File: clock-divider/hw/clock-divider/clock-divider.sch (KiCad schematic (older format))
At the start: 48 parts

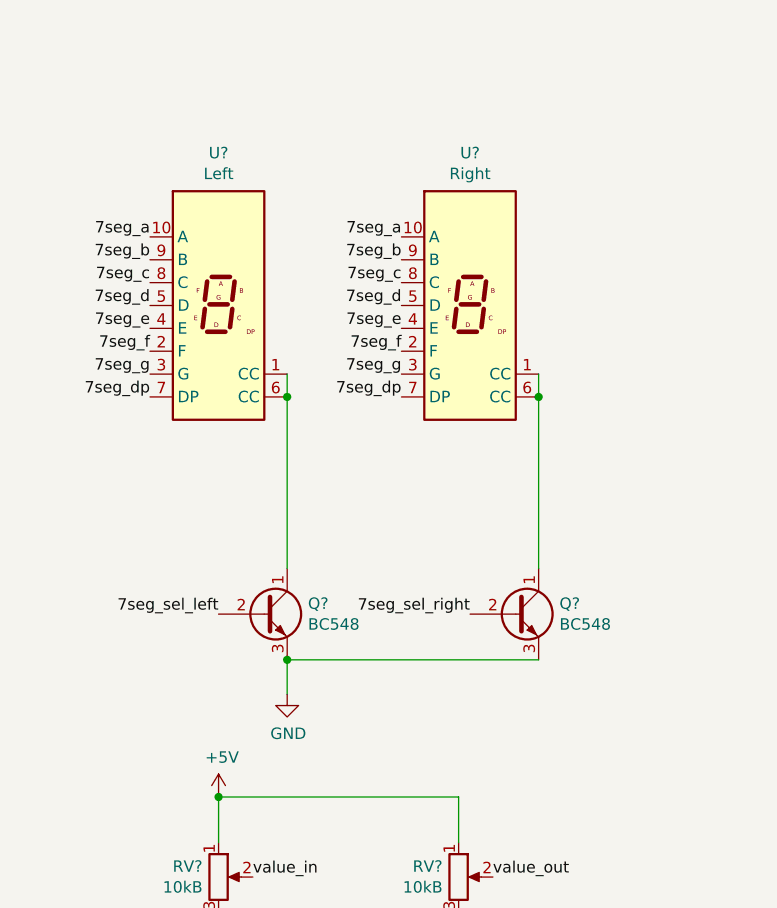
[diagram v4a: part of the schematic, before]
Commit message: clock-divider: change 7 segment display to common anode
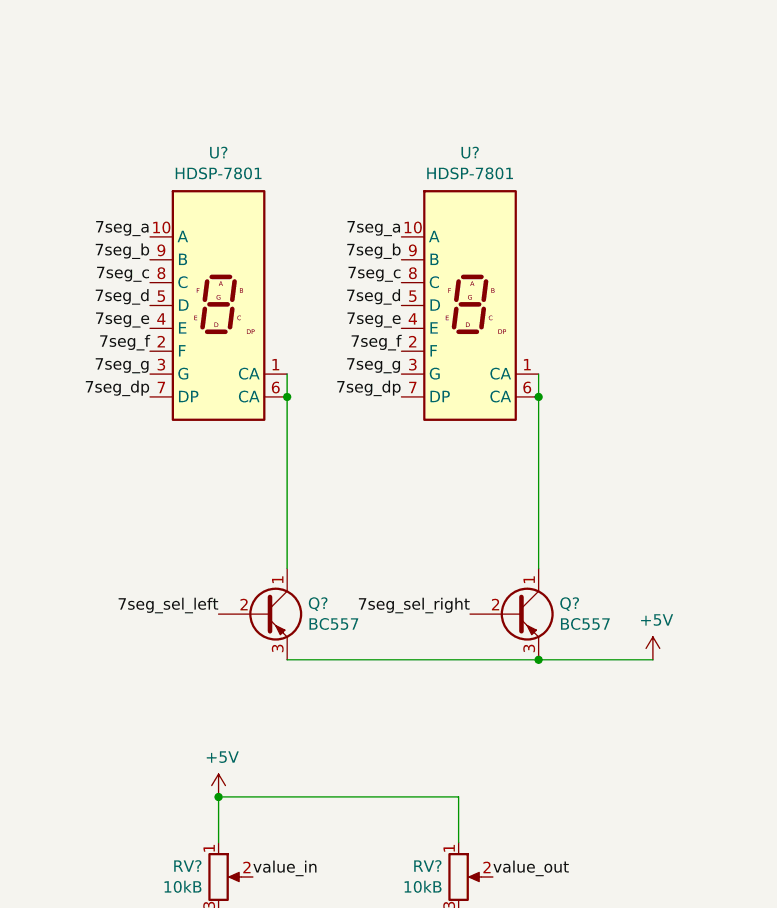
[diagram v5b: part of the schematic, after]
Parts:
- removed Q? (x2): BC548, Package_TO_SOT_THT:TO-92_Inline, symbol Transistor_BJT:BC548
- removed U?: Left, Display_7Segment:HDSP-7801, symbol Display_Character:HDSP-7803
- removed U?: Right, Display_7Segment:HDSP-7801, symbol Display_Character:HDSP-7803
- added Q? (x2): BC557, Package_TO_SOT_THT:TO-92_Inline, symbol Transistor_BJT:BC557
- added U? (x2): HDSP-7801, Display_7Segment:HDSP-7801, symbol Display_Character:HDSP-7801
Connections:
- net +5V: now also Q?.3 (E), Q?.3 (E)
- net 7seg_a: now also U?.10 (A), U?.10 (A)
- net 7seg_b: now also U?.9 (B), U?.9 (B)
- net 7seg_c: now also U?.8 (C), U?.8 (C)
- net 7seg_d: now also U?.5 (D), U?.5 (D)
- net 7seg_dp: now also U?.7 (DP), U?.7 (DP)
- net 7seg_e: now also U?.4 (E), U?.4 (E)
- net 7seg_f: now also U?.2 (F), U?.2 (F)
- net 7seg_g: now also U?.3 (G), U?.3 (G)
- net 7seg_sel_left: now also Q?.2 (B)
- net 7seg_sel_right: now also Q?.2 (B)
- new net: Q?.1 (C), U?.1 (CA), U?.6 (CA) (x2)
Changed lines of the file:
@@
 Connection ~ 4400 1500
-$Comp
-L Display_Character:HDSP-7803 U?
-U 1 1 60601416
-P 8550 2100
-F 0 "U?" H 8550 2767 50  0000 C CNN
-F 1 "Left" H 8550 2676 50  0000 C CNN
-F 2 "Display_7Segment:HDSP-7801" H 8550 1550 50  0001 C CNN
-F 3 "https://docs.broadcom.com/docs/AV02-2553EN" H 8550 2100 50  0001 C CNN
-	1    8550 2100
-	1    0    0    -1
-$EndComp
-$Comp
-L Display_Character:HDSP-7803 U?
-U 1 1 60603731
-P 9650 2100
-F 0 "U?" H 9650 2767 50  0000 C CNN
-F 1 "Right" H 9650 2676 50  0000 C CNN
-F 2 "Display_7Segment:HDSP-7801" H 9650 1550 50  0001 C CNN
-F 3 "https://docs.broadcom.com/docs/AV02-2553EN" H 9650 2100 50  0001 C CNN
-	1    9650 2100
-	1    0    0    -1
-$EndComp
-$Comp
-L Transistor_BJT:BC548 Q?
-U 1 1 60604B60
-P 8750 3450
-F 0 "Q?" H 8941 3496 50  0000 L CNN
-F 1 "BC548" H 8941 3405 50  0000 L CNN
-F 2 "Package_TO_SOT_THT:TO-92_Inline" H 8950 3375 50  0001 L CIN
-F 3 "https://www.onsemi.com/pub/Collateral/BC550-D.pdf" H 8750 3450 50  0001 L CNN
-	1    8750 3450
-	1    0    0    -1
-$EndComp
-$Comp
-L Transistor_BJT:BC548 Q?
-U 1 1 60605442
-P 9850 3450
-F 0 "Q?" H 10041 3496 50  0000 L CNN
-F 1 "BC548" H 10041 3405 50  0000 L CNN
-F 2 "Package_TO_SOT_THT:TO-92_Inline" H 10050 3375 50  0001 L CIN
-F 3 "https://www.onsemi.com/pub/Collateral/BC550-D.pdf" H 9850 3450 50  0001 L CNN
-	1    9850 3450
-	1    0    0    -1
-$EndComp
 $Comp
 L Device:R_POT RV?
@@
 Text Label 9400 5650 2    50   ~ 0
 act_out
-Wire Wire Line
-	8850 2400 8850 2500
-Connection ~ 8850 2500
-Wire Wire Line
-	9950 3250 9950 2500
-Connection ~ 9950 2500
-Wire Wire Line
-	9950 2500 9950 2400
 Text Label 9350 1800 2    50   ~ 0
 7seg_a
@@
 Text Label 10400 5650 2    50   ~ 0
 disp_next_seq
-$Comp
-L power:GND #PWR?
-U 1 1 6078B251
-P 8850 3800
-F 0 "#PWR?" H 8850 3550 50  0001 C CNN
-F 1 "GND" H 8855 3627 50  0000 C CNN
-F 2 "" H 8850 3800 50  0001 C CNN
-F 3 "" H 8850 3800 50  0001 C CNN
-	1    8850 3800
-	1    0    0    -1
-$EndComp
 Wire Wire Line
 	9950 3650 8850 3650
-Wire Wire Line
-	8850 3650 8850 3800
-Connection ~ 8850 3650
 $Comp
 L Device:R R?
@@
 	0    1    1    0
 $EndComp
-Wire Wire Line
-	8850 2500 8850 3250
 Text Label 9650 3450 2    50   ~ 0
 7seg_sel_right
@@
 NoConn ~ 1150 1100
 NoConn ~ 1150 1200
+$Comp
+L Display_Character:HDSP-7801 U?
+U 1 1 60924FDA
+P 9650 2100
+F 0 "U?" H 9650 2767 50  0000 C CNN
+F 1 "HDSP-7801" H 9650 2676 50  0000 C CNN
+F 2 "Display_7Segment:HDSP-7801" H 9650 1550 50  0001 C CNN
+F 3 "https://docs.broadcom.com/docs/AV02-2553EN" H 9650 2100 50  0001 C CNN
+	1    9650 2100
+	1    0    0    -1
+$EndComp
+Wire Wire Line
+	9950 2500 9950 3250
+Wire Wire Line
+	9950 2400 9950 2500
+Connection ~ 9950 2500
+$Comp
+L Display_Character:HDSP-7801 U?
+U 1 1 6092EEE8
+P 8550 2100
+F 0 "U?" H 8550 2767 50  0000 C CNN
+F 1 "HDSP-7801" H 8550 2676 50  0000 C CNN
+F 2 "Display_7Segment:HDSP-7801" H 8550 1550 50  0001 C CNN
+F 3 "https://docs.broadcom.com/docs/AV02-2553EN" H 8550 2100 50  0001 C CNN
+	1    8550 2100
+	1    0    0    -1
+$EndComp
+Wire Wire Line
+	8850 2500 8850 3250
+Wire Wire Line
+	8850 2400 8850 2500
+Connection ~ 8850 2500
+$Comp
+L Transistor_BJT:BC557 Q?
+U 1 1 60932F7D
+P 8750 3450
+F 0 "Q?" H 8941 3496 50  0000 L CNN
+F 1 "BC557" H 8941 3405 50  0000 L CNN
+F 2 "Package_TO_SOT_THT:TO-92_Inline" H 8950 3375 50  0001 L CIN
+F 3 "https://www.onsemi.com/pub/Collateral/BC556BTA-D.pdf" H 8750 3450 50  0001 L CNN
+	1    8750 3450
+	1    0    0    -1
+$EndComp
+$Comp
+L Transistor_BJT:BC557 Q?
+U 1 1 60933AFE
+P 9850 3450
+F 0 "Q?" H 10041 3496 50  0000 L CNN
+F 1 "BC557" H 10041 3405 50  0000 L CNN
+F 2 "Package_TO_SOT_THT:TO-92_Inline" H 10050 3375 50  0001 L CIN
+F 3 "https://www.onsemi.com/pub/Collateral/BC556BTA-D.pdf" H 9850 3450 50  0001 L CNN
+	1    9850 3450
+	1    0    0    -1
+$EndComp
+$Comp
+L power:+5V #PWR?
+U 1 1 60935CE1
+P 10450 3650
+F 0 "#PWR?" H 10450 3500 50  0001 C CNN
+F 1 "+5V" H 10465 3823 50  0000 C CNN
+F 2 "" H 10450 3650 50  0001 C CNN
+F 3 "" H 10450 3650 50  0001 C CNN
+	1    10450 3650
+	1    0    0    -1
+$EndComp
+Wire Wire Line
+	9950 3650 10450 3650
+Connection ~ 9950 3650
 $EndSCHEMATC

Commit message: clock-divider: hw: add symbol for another 7 segment display
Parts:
- removed U? (x2): HDSP-7801, Display_7Segment:HDSP-7801, symbol Display_Character:HDSP-7801
- added U? (x2): SA52-11EWA, Display_7Segment:Sx52-1xxxxx, symbol special-parts:SA52-11EWA
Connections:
- net 7seg_a: now also U?.7 (A), U?.7 (A)
- net 7seg_b: now also U?.6 (B), U?.6 (B)
- net 7seg_c: now also U?.4 (C), U?.4 (C)
- net 7seg_d: now also U?.2 (D), U?.2 (D)
- net 7seg_dp: now also U?.5 (DP), U?.5 (DP)
- net 7seg_e: now also U?.1 (E), U?.1 (E)
- net 7seg_f: now also U?.9 (F), U?.9 (F)
- net 7seg_g: now also U?.10 (G), U?.10 (G)
- net at Q?.1 (C): now also U?.3 (CA), U?.8 (CA) (x2)
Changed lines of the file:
@@
 NoConn ~ 1150 1200
-$Comp
-L Display_Character:HDSP-7801 U?
-U 1 1 60924FDA
-P 9650 2100
-F 0 "U?" H 9650 2767 50  0000 C CNN
-F 1 "HDSP-7801" H 9650 2676 50  0000 C CNN
-F 2 "Display_7Segment:HDSP-7801" H 9650 1550 50  0001 C CNN
-F 3 "https://docs.broadcom.com/docs/AV02-2553EN" H 9650 2100 50  0001 C CNN
-	1    9650 2100
-	1    0    0    -1
-$EndComp
-Wire Wire Line
-	9950 2500 9950 3250
-Wire Wire Line
-	9950 2400 9950 2500
-Connection ~ 9950 2500
-$Comp
-L Display_Character:HDSP-7801 U?
-U 1 1 6092EEE8
-P 8550 2100
-F 0 "U?" H 8550 2767 50  0000 C CNN
-F 1 "HDSP-7801" H 8550 2676 50  0000 C CNN
-F 2 "Display_7Segment:HDSP-7801" H 8550 1550 50  0001 C CNN
-F 3 "https://docs.broadcom.com/docs/AV02-2553EN" H 8550 2100 50  0001 C CNN
-	1    8550 2100
-	1    0    0    -1
-$EndComp
-Wire Wire Line
-	8850 2500 8850 3250
-Wire Wire Line
-	8850 2400 8850 2500
-Connection ~ 8850 2500
 $Comp
 L Transistor_BJT:BC557 Q?
@@
 	9950 3650 10450 3650
 Connection ~ 9950 3650
+$Comp
+L special-parts:SA52-11EWA U?
+U 1 1 6096ED5D
+P 9650 2100
+F 0 "U?" H 9650 2767 50  0000 C CNN
+F 1 "SA52-11EWA" H 9650 2676 50  0000 C CNN
+F 2 "Display_7Segment:Sx52-1xxxxx" H 9650 1550 50  0001 C CNN
+F 3 "http://www.kingbrightusa.com/images/catalog/SPEC/sa52-11ewa.pdf" H 9650 2100 50  0001 C CNN
+	1    9650 2100
+	1    0    0    -1
+$EndComp
+Wire Wire Line
+	9950 2500 9950 3250
+Wire Wire Line
+	9950 2400 9950 2500
+Connection ~ 9950 2500
+$Comp
+L special-parts:SA52-11EWA U?
+U 1 1 6097A638
+P 8550 2100
+F 0 "U?" H 8550 2767 50  0000 C CNN
+F 1 "SA52-11EWA" H 8550 2676 50  0000 C CNN
+F 2 "Display_7Segment:Sx52-1xxxxx" H 8550 1550 50  0001 C CNN
+F 3 "http://www.kingbrightusa.com/images/catalog/SPEC/sa52-11ewa.pdf" H 8550 2100 50  0001 C CNN
+	1    8550 2100
+	1    0    0    -1
+$EndComp
+Wire Wire Line
+	8850 2500 8850 3250
+Wire Wire Line
+	8850 2400 8850 2500
+Connection ~ 8850 2500
 $EndSCHEMATC

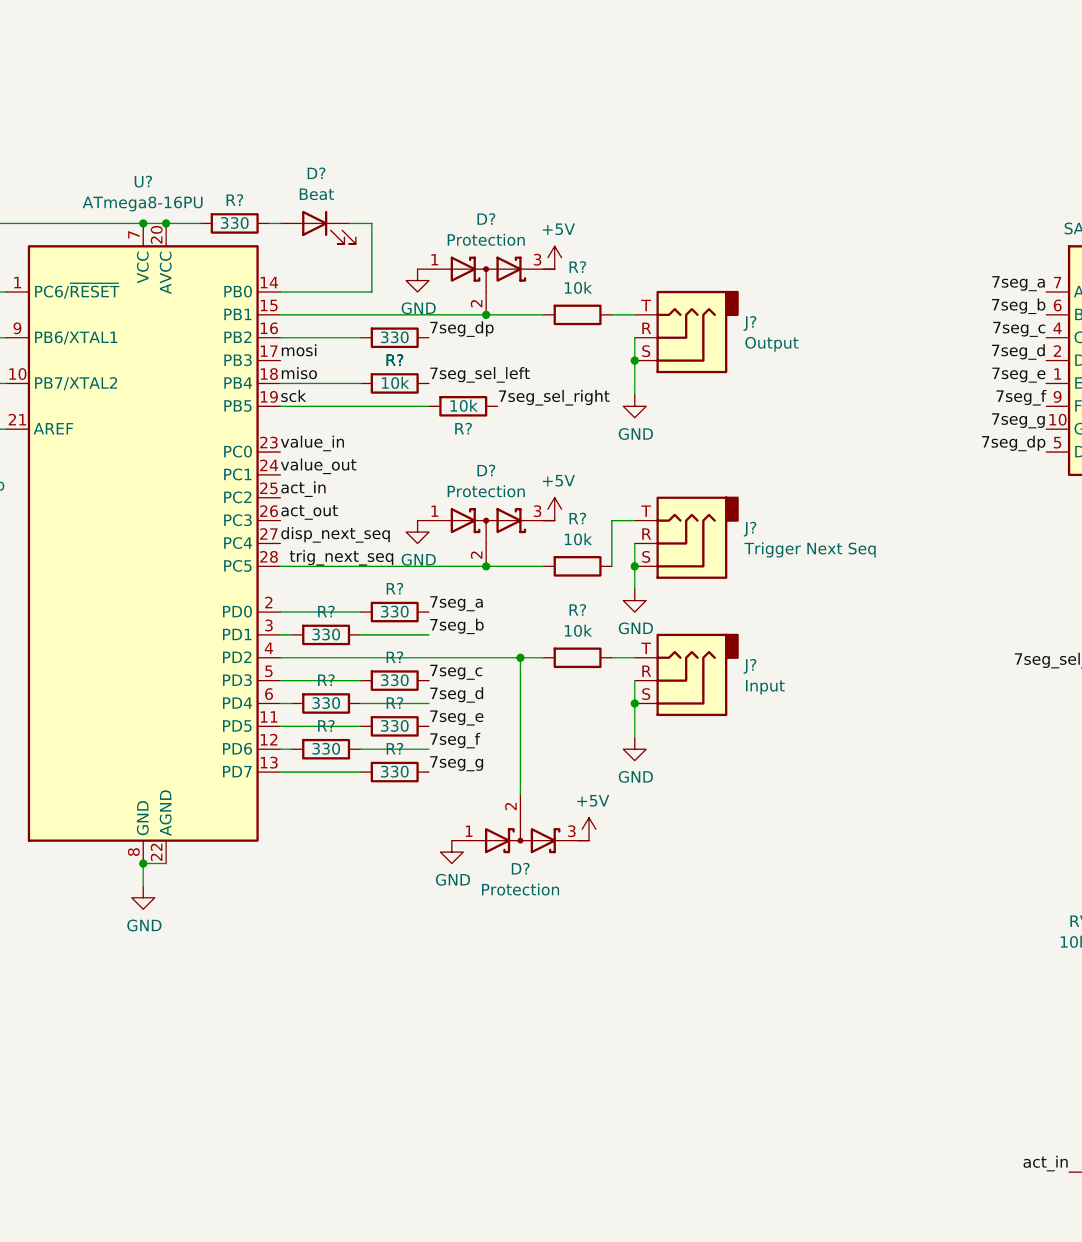
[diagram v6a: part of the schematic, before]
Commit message: clock-divider: hw: change several pins, sacrificing BEAT LED for MIDI
Apart from freeing up USART pins PD[0,1] for potential use for MIDI,
this change has further benefits:
  - trigger input is now connected to INT1, which might come in handy
  - 7 seg outputs are now separated in nibbles and in order, which
    allows easier bitmasks
The downsides are losing the beat LED, which can be substituted by
blinking the 7-segs' decimal points and mixing inputs and outputs more
across registers, which is only of cosmetic concern.

All pins are now in use and all ISP pins are now shared. \o/
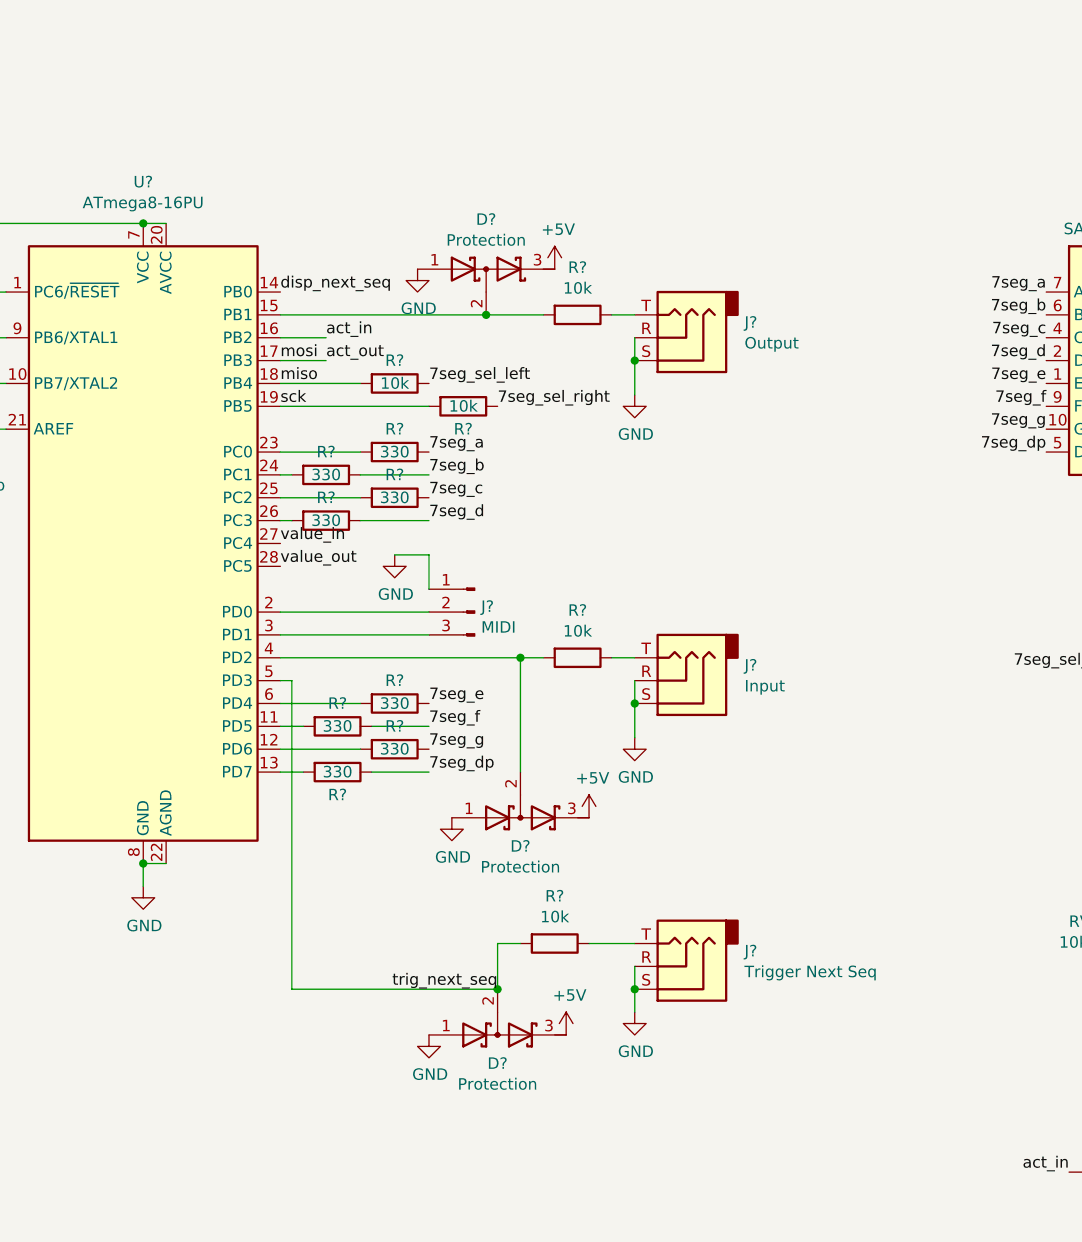
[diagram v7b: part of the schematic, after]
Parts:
- removed D?: Beat, symbol Device:LED
- removed R?: 330, symbol Device:R
- added J?: MIDI, symbol Connector:Conn_01x03_Male
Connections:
- net mosi is gone; now on net act_out: R?.1, U?.17 (PB3)
- net GND: now also J?.1 (Pin_1)
- net act_in: now also U?.16 (PB2); no longer U?.25 (PC2)
- net act_out: no longer U?.26 (PC3)
- net disp_next_seq: now also U?.14 (PB0); no longer U?.27 (PC4)
- net trig_next_seq: now also U?.5 (PD3); no longer U?.28 (PC5)
- net value_in: now also U?.27 (PC4); no longer U?.23 (PC0)
- net value_out: now also U?.28 (PC5); no longer U?.24 (PC1)
- net at U?.11 (PD5): now also R?.2; no longer R?.2
- net at U?.12 (PD6): now also R?.2; no longer R?.2
- net at U?.13 (PD7): now also R?.2; no longer R?.2
- net at U?.2 (PD0): now also J?.2 (Pin_2); no longer R?.2
- net at R?.2: now also U?.24 (PC1); no longer U?.3 (PD1)
- net at R?.2: now also U?.25 (PC2); no longer U?.5 (PD3)
- net at R?.2: now also U?.26 (PC3); no longer U?.6 (PD4)
- new net: R?.2, U?.23 (PC0)
- new net: J?.3 (Pin_3), U?.3 (PD1)
- new net: R?.2, U?.6 (PD4)
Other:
- moved on the sheet: D?, J?, R?
